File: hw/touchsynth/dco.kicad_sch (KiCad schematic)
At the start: 20 parts, among them Q1 MMBT3904, Q2 2N7002, Q3 MMBT3904, U11 TL072, U12 LM324

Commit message: Schematic v2: hand-drawn sheet layouts with wires; MIDI in DNP
- draw.py/gen_sch2.py/layouts.py: placement + wiring per block, automatic
  labels for remaining split nets, short detection, junctions, KiCad
  endpoint-only connection semantics
- all 7 sheets laid out (ladder drawn as a transistor stack, diff amps,
  integrator with reset, R-2R DAC, ...); ERC 0 violations, netlist == design,
  145 simulated elements match
- MIDI input parts marked DNP (footprints kept)
- docs/touchsynth_schematic.pdf

Co-Authored-By: Claude Opus 5.5 (1M context) <noreply@anthropic.com>
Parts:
- added C45: 100n, Capacitor_SMD:C_0603_1608Metric, symbol Device:C
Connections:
- net GND: now also C45.2
- net VP: now also C45.1
- net CVA_A: no longer names the net of C22.1, R32.2, R33.1
- net CVA_B: no longer names the net of C23.1, R33.2, R34.1
- net DCO_B2: no longer names the net of Q3.1 (B), R40.2
- net DCO_GATE: no longer names the net of Q2.1 (G), R38.2
- net DCO_GD: no longer names the net of Q3.3 (C), R38.1, R39.2
- net VIA_B: no longer names the net of Q1.1 (B), R36.2
- net VIA_E: no longer names the net of Q1.2 (E), R37.1, U12.2 (-)
- net VIA_OUT: no longer names the net of R36.1, U12.1
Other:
- note added: "CV_AMP: PWM filter and V-to-I converter (charge current proportional to the note frequency)"
- note added: "Integrator (TL072) with 2N7002 reset and NPN gate level shifter"
- note removed: "CV_AMP filter and V-to-I converter"
- note removed: "Integrator and reset"
- note removed: "Test points"

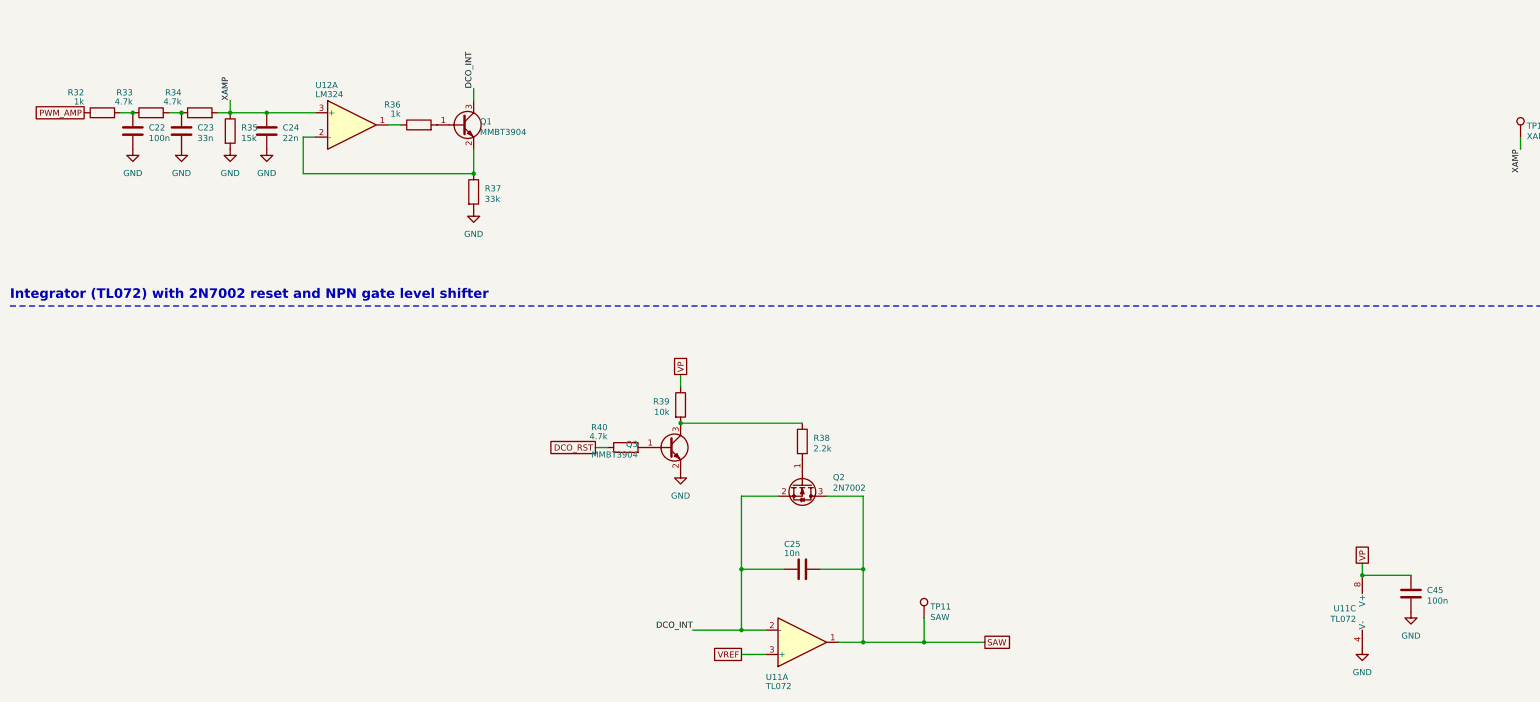
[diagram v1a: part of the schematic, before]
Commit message: PCB placement by functional block, silkscreen art, discrete LED resistors
- gen_pcb.py / pcb_place.py: 100 x 100 mm 2-layer board; keys, LEDs, connectors and test points fixed,
  ICs anchored per block, remaining parts placed greedily by connectivity inside their block
- blocks tile the circuit area with a 0.35 mm street for the dashed silkscreen frames and a reserved
  title tab each (pcb_art.py); piano keybed with hatched black keys; logo, resonant saw and ladder
  response curves on the front; signal-flow diagram on the back
- LED resistor arrays replaced by 16 discrete 4.7k 0603 (basic part) next to each LED
- deterministic schematic UUIDs, net name labels for PCB parity, op-amp re-pairing, fab.py

Co-Authored-By: Claude Opus 5.5 (1M context) <noreply@anthropic.com>
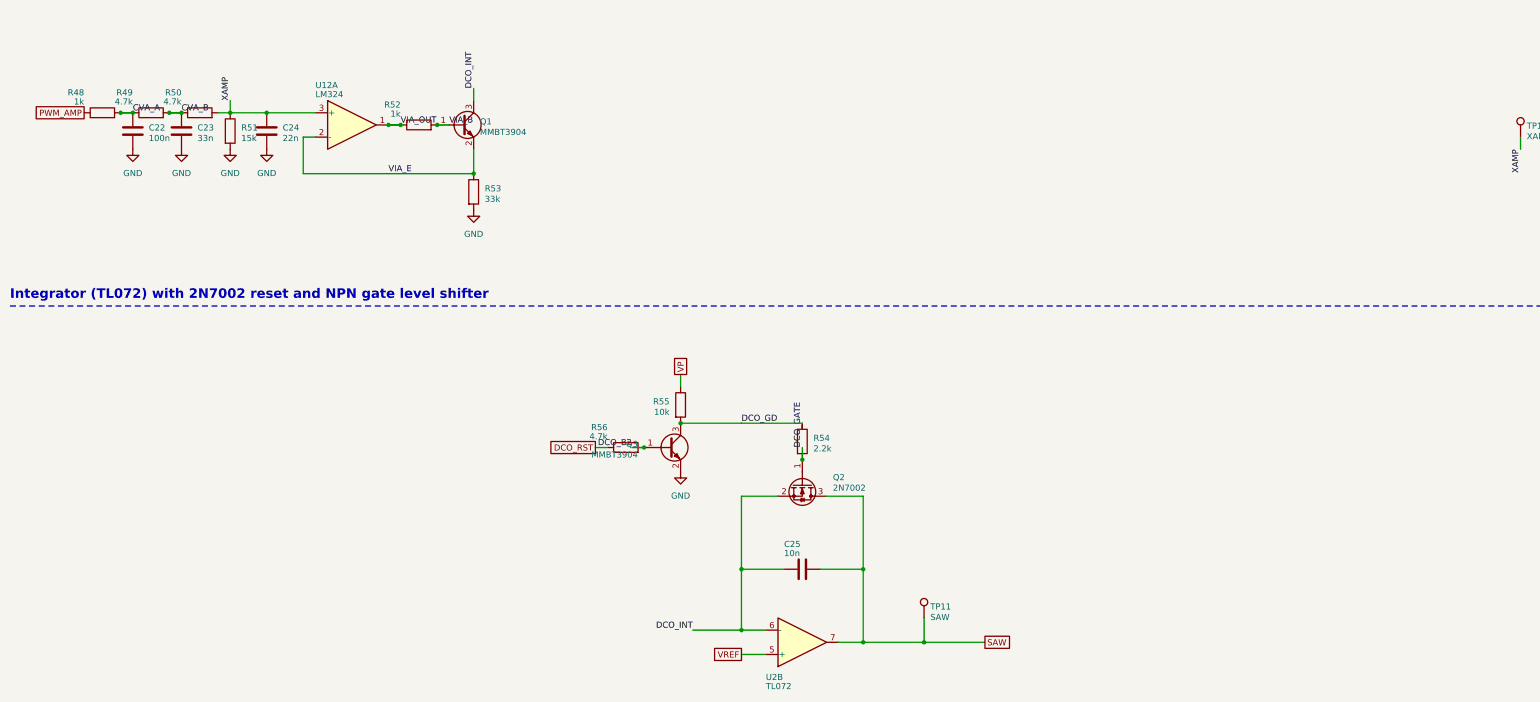
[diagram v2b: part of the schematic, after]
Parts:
- removed C45: 100n, Capacitor_SMD:C_0603_1608Metric, symbol Device:C
- removed R32, R36: 1k, Resistor_SMD:R_0603_1608Metric, symbol Device:R
- removed R33, R34, R40: 4.7k, Resistor_SMD:R_0603_1608Metric, symbol Device:R
- removed R35: 15k, Resistor_SMD:R_0603_1608Metric, symbol Device:R
- removed R37: 33k, Resistor_SMD:R_0603_1608Metric, symbol Device:R
- removed R38: 2.2k, Resistor_SMD:R_0603_1608Metric, symbol Device:R
- removed R39: 10k, Resistor_SMD:R_0603_1608Metric, symbol Device:R
- removed U11: TL072, Package_SO:SOIC-8_3.9x4.9mm_P1.27mm, symbol Amplifier_Operational:TL072
- added R48, R52: 1k, Resistor_SMD:R_0603_1608Metric, symbol Device:R
- added R49, R50, R56: 4.7k, Resistor_SMD:R_0603_1608Metric, symbol Device:R
- added R51: 15k, Resistor_SMD:R_0603_1608Metric, symbol Device:R
- added R53: 33k, Resistor_SMD:R_0603_1608Metric, symbol Device:R
- added R54: 2.2k, Resistor_SMD:R_0603_1608Metric, symbol Device:R
- added R55: 10k, Resistor_SMD:R_0603_1608Metric, symbol Device:R
- added U2: TL072, Package_SO:SOIC-8_3.9x4.9mm_P1.27mm, symbol Amplifier_Operational:TL072
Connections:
- net DCO_INT: now also U2.6 (-)
- net DCO_RST: now also R56.1
- net GND: now also R51.2, R53.2
- net PWM_AMP: now also R48.1
- net SAW: now also U2.7
- net VP: now also R55.1
- net VREF: now also U2.5 (+)
- net XAMP: now also R50.2, R51.1
- net DCO_GATE: now reaches Q2.1 (G)
- net DCO_GATE: now also R54.2
- net DCO_B2: now reaches Q3.1 (B)
- net DCO_B2: now also R56.2
- net DCO_GD: now reaches Q3.3 (C)
- net DCO_GD: now also R54.1, R55.2
- net VIA_OUT: now reaches U12.1
- net VIA_OUT: now also R52.1
- net VIA_B: now reaches Q1.1 (B)
- net VIA_B: now also R52.2
- net VIA_E: now reaches Q1.2 (E), U12.2 (-)
- net VIA_E: now also R53.1
- net CVA_A: now reaches C22.1
- net CVA_A: now also R48.2, R49.1
- net CVA_B: now reaches C23.1
- net CVA_B: now also R49.2, R50.1

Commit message: 4-layer PCB: keys I/O row, trim DAC by the VCA, full routing and fab outputs
- 4 layers: F.Cu signals, In1 solid GND, In2 split power (VP analog / +5V digital / GND under the keys),
  B.Cu signals; no plane and no foreign tracks under the touch pads
- floorplan: analog blocks 72 x 36 mm in signal-flow order, right column MIDI / trim DAC / MCU,
  keys I/O row (touch muxes, LED shift registers) directly above the keys; shorter white keys,
  function pads flush with the keybed; test points inside their blocks, two THT scope-ground pins
- routing pipeline: plane stitch vias, pre-routed plane nets, Freerouting, GND via grid, island
  check, A* maze router for leftovers (pcb_maze.py), rip-up repair mode
- DRC: 0 violations, 0 unconnected, schematic parity OK; JLCPCB gerbers / BOM / CPL via fab.py
- silkscreen: back-side credits (design: cpldcpu & Claude Opus 5.5), vias kept out of the art

Co-Authored-By: Claude Opus 5.5 (1M context) <noreply@anthropic.com>
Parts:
- removed TP11: SAW, TestPoint:TestPoint_Pad_D1.0mm, symbol Connector:TestPoint
- added TP13: XAMP, TestPoint:TestPoint_Pad_D1.0mm, symbol Connector:TestPoint
- TP12: value XAMP -> SAW
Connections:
- net SAW: now also TP12.1
- net XAMP: now also TP13.1; no longer TP12.1
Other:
- moved on the sheet: TP12
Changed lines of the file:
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@@
 		(on_board yes)
 		(dnp no)
-		(property "Reference" "TP11"
+		(property "Reference" "TP12"
 			(at 207.04 158.939 0)
 			(effects
@@
 			(project "touchsynth"
 				(path "/c42cd0d4-93b1-5178-97ee-fdd3025be2c6/8bf3fd65-1014-59d1-af23-d9d8de8de856"
-					(reference "TP11")
+					(reference "TP12")
 					(unit 1)
 				)
@@
 		(on_board yes)
 		(dnp no)
-		(property "Reference" "TP12"
+		(property "Reference" "TP13"
 			(at 331.5 58.609 0)
 			(effects
@@
 			(project "touchsynth"
 				(path "/c42cd0d4-93b1-5178-97ee-fdd3025be2c6/8bf3fd65-1014-59d1-af23-d9d8de8de856"
-					(reference "TP12")
-					(unit 1)
-				)
+					(reference "TP13")
+					(unit 1)
+				)
